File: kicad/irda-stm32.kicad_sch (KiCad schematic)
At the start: 33 parts, among them J1 USB_C_Receptacle_USB2.0_16P, J2 UART, J3 SWD, SW1 BOOT0_BUT, SW2 NRST_BUT, U1 TLV1117LV33DCYR, U2 STM32F042K6Tx, U3 TFBS4711

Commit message: update kicad, idk
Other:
- note added: "Alternative STM32C071FBP6 Slightly better/cheaper part but F042 is more available. F042Fxxx overlaps USB/UART1 which means its unuseable."
- note removed: "Alternative STM32C071FBPx Slightly better/cheaper part but F042 is more available. F042F overlaps USB/UART1 which means its unuseable."
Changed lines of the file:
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@@
 		)
 	)
-	(text "Alternative\nSTM32C071FBPx\n\nSlightly better/cheaper part but F042 is more available.\n\nF042F overlaps USB/UART1 which means its unuseable."
+	(text "Alternative\nSTM32C071FBP6\n\nSlightly better/cheaper part but F042 is more available.\n\nF042Fxxx overlaps USB/UART1 which means its unuseable."
 		(exclude_from_sim no)
 		(at 102.362 147.32 0)

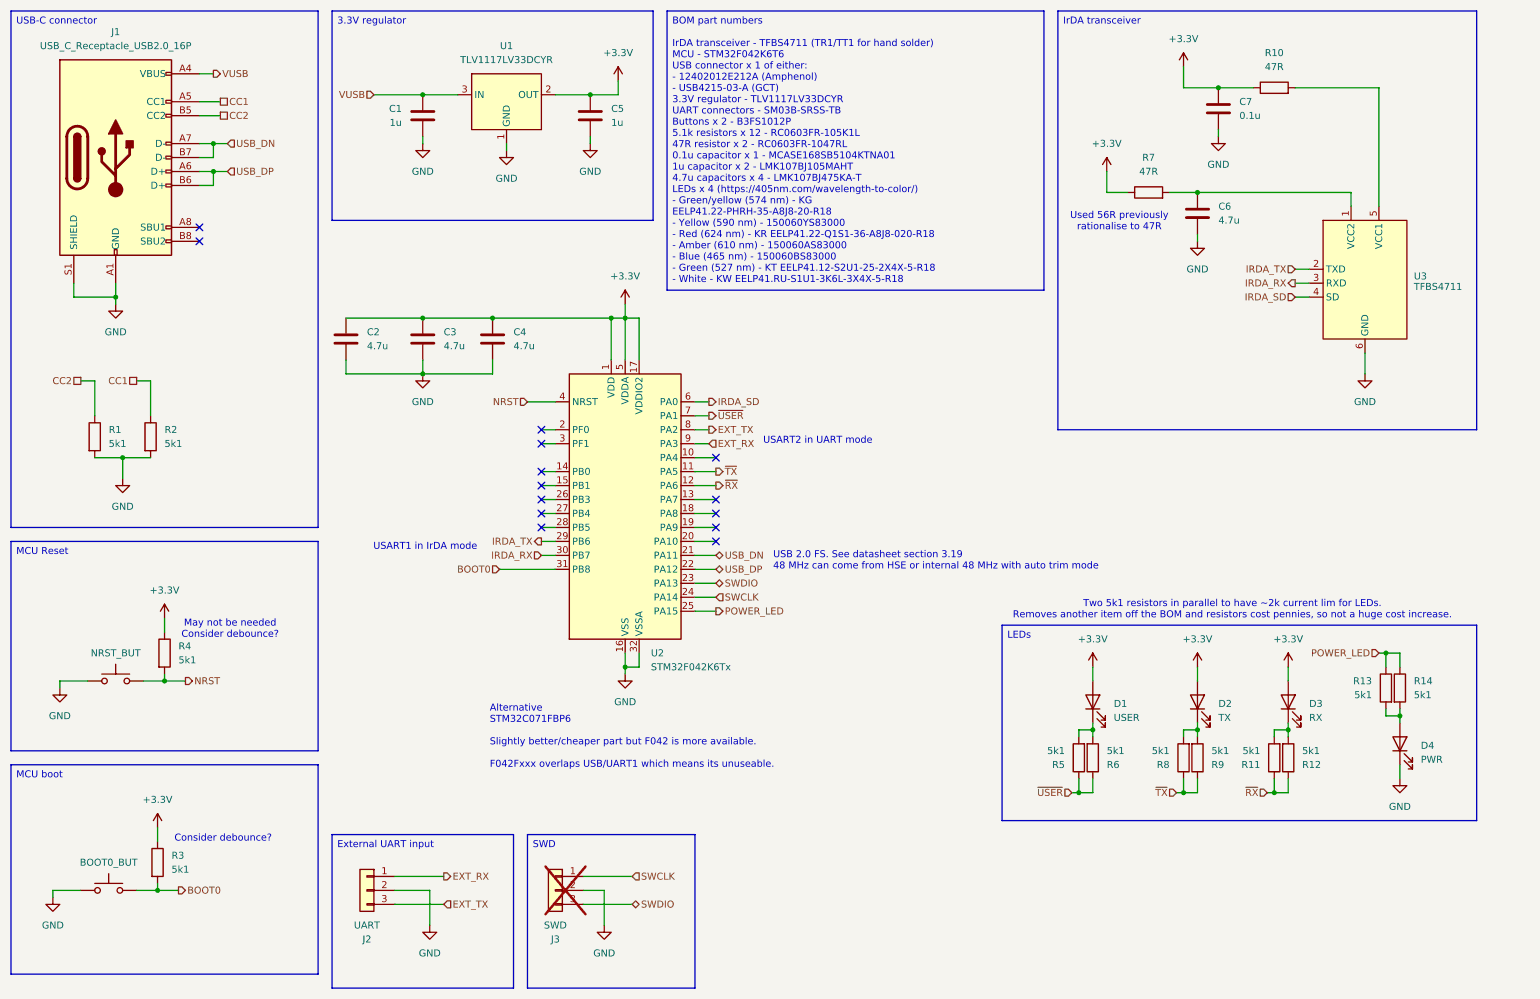
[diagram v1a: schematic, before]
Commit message: update PCB for c071fbp6
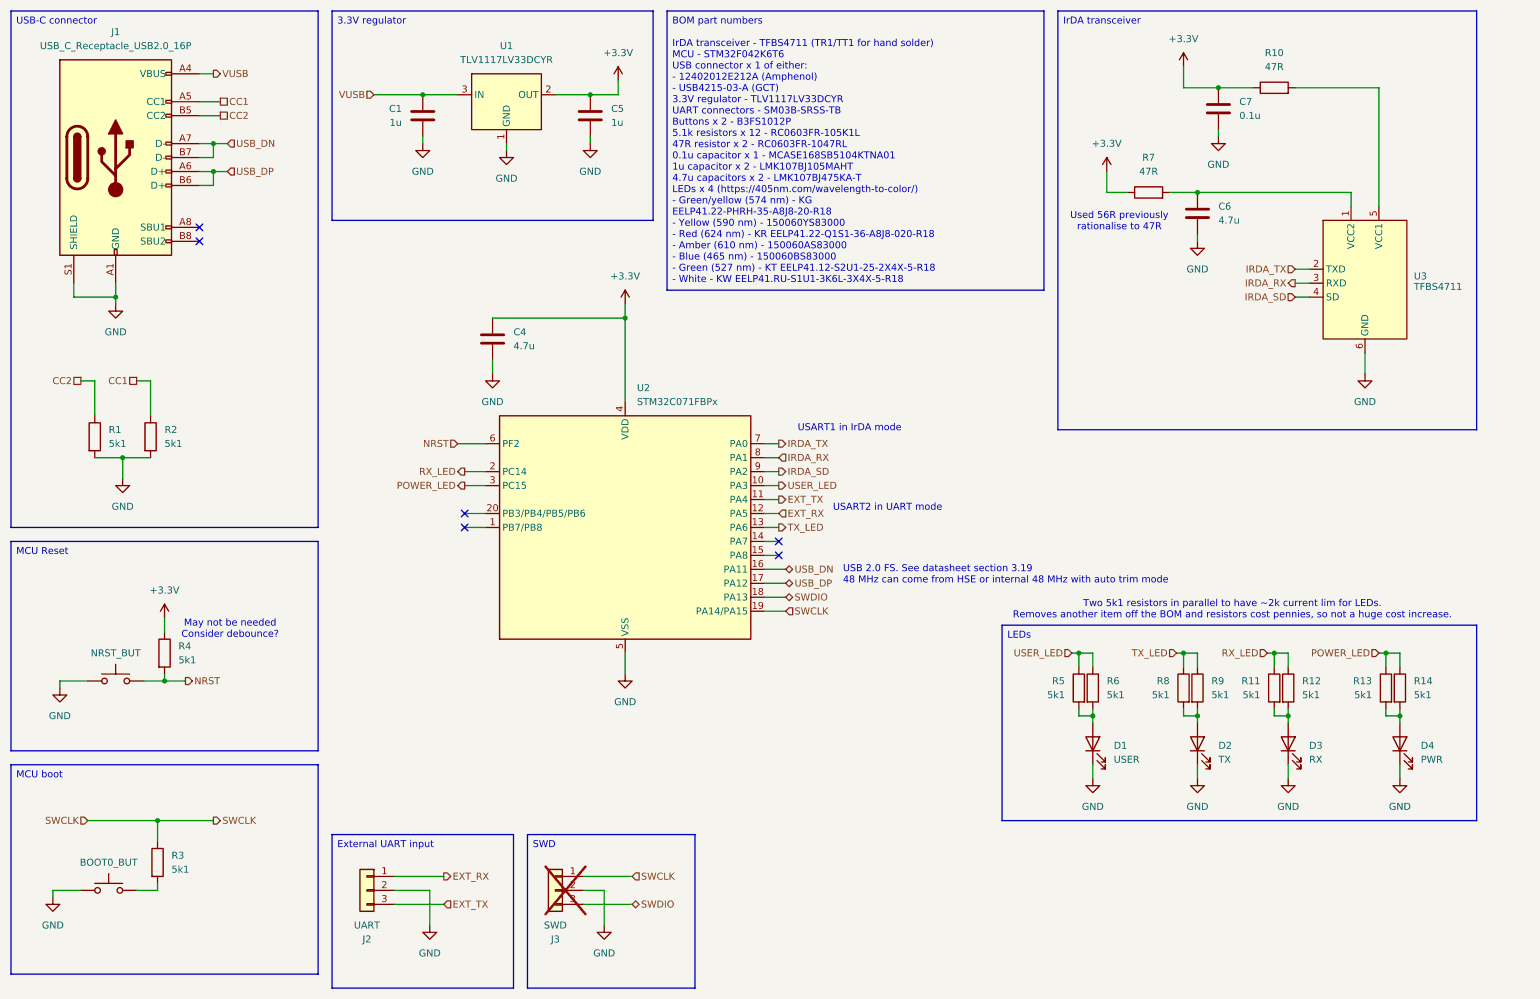
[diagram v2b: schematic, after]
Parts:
- removed C2, C3: 4.7u, Capacitor_SMD:C_0603_1608Metric, symbol Device:C
- removed U2: STM32F042K6Tx, Package_QFP:LQFP-32_7x7mm_P0.8mm, symbol MCU_ST_STM32F0:STM32F042K6Tx
- added U2: STM32C071FBPx, Package_SO:TSSOP-20_4.4x6.5mm_P0.65mm, symbol MCU_ST_STM32C0:STM32C071FBPx
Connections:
- net +3.3V: now also U2.4 (VDD); no longer D1.2 (A), D2.2 (A), D3.2 (A), R3.1
- net EXT_RX: now also U2.12 (PA5)
- net EXT_TX: now also U2.11 (PA4)
- net GND: now also D1.1 (K), D2.1 (K), D3.1 (K), U2.5 (VSS)
- net IRDA_RX: now also U2.8 (PA1)
- net IRDA_SD: now also U2.9 (PA2)
- net IRDA_TX: now also U2.7 (PA0)
- net NRST: now also U2.6 (PF2)
- net POWER_LED: now also U2.3 (PC15)
- net SWCLK: now also R3.1, U2.19 (PA14/PA15)
- net SWDIO: now also U2.18 (PA13)
- net USB_DN: now also U2.16 (PA11)
- net USB_DP: now also U2.17 (PA12)
- net at R8.2, R9.2: now also D2.2 (A); no longer D2.1 (K)
- net at R5.2, R6.2: now also D1.2 (A); no longer D1.1 (K)
- net at R11.2, R12.2: now also D3.2 (A); no longer D3.1 (K)
- net BOOT0: no longer names the net of R3.2, SW1.2
- net ~{RX} renamed RX_LED
- net RX_LED: now also U2.2 (PC14)
- net ~{TX} renamed TX_LED
- net TX_LED: now also U2.13 (PA6)
- net ~{USER} renamed USER_LED
- net USER_LED: now also U2.10 (PA3)
- no-connect marks 14 -> 6
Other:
- note removed: "Alternative STM32C071FBP6 Slightly better/cheaper part but F042 is more available. F042Fxxx overlaps USB/UART1 which means its unuseable."
- note removed: "Consider debounce?"
- moved on the sheet: D1, D2, D3, R11, R12, R5, R6, R8, R9

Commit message: fix BOOT0 button and USB ground
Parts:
- added C6: 0.1u, Capacitor_SMD:C_0603_1608Metric, symbol Device:C
- added TP1: NRST, Connector_PinHeader_2.54mm:PinHeader_1x01_P2.54mm_Vertical, symbol Connector:TestPoint
- renumbered C7 to C1, C6 to C2, C1 to C3, C5 to C4, C4 to C5, R10 to R1, R11 to R10, R12 to R11, R13 to R12, R14 to R13, R3 to R14, R7 to R2, R1 to R3, R2 to R4, R4 to R5, R5 to R6, R6 to R7, SW2 to SW1, SW1 to SW2, U3 to U2, U2 to U3
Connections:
- net +3.3V: now also SW2.2
- net GND: now also R14.2, C6.2; no longer SW2.1
- net NRST: now also C6.1, TP1.1
- net SWCLK: now also SW2.1
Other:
- note removed: "May not be needed Consider debounce?"
- moved on the sheet: R14, R5

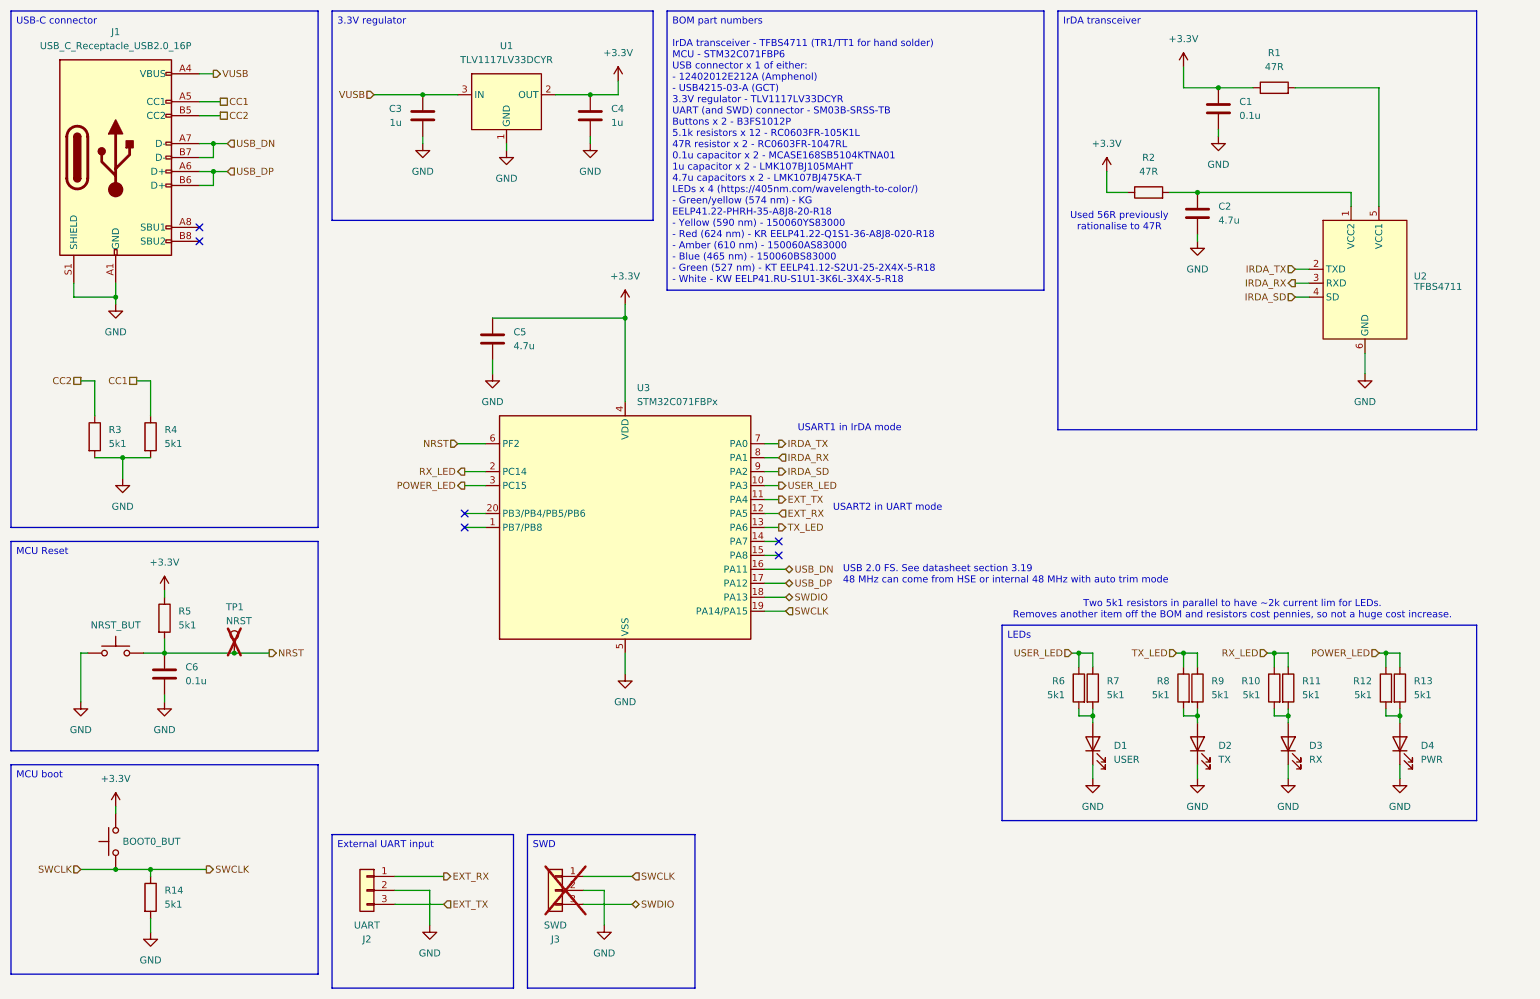
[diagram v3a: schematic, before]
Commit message: add lcsc/jlc part numbers and fix ir filters
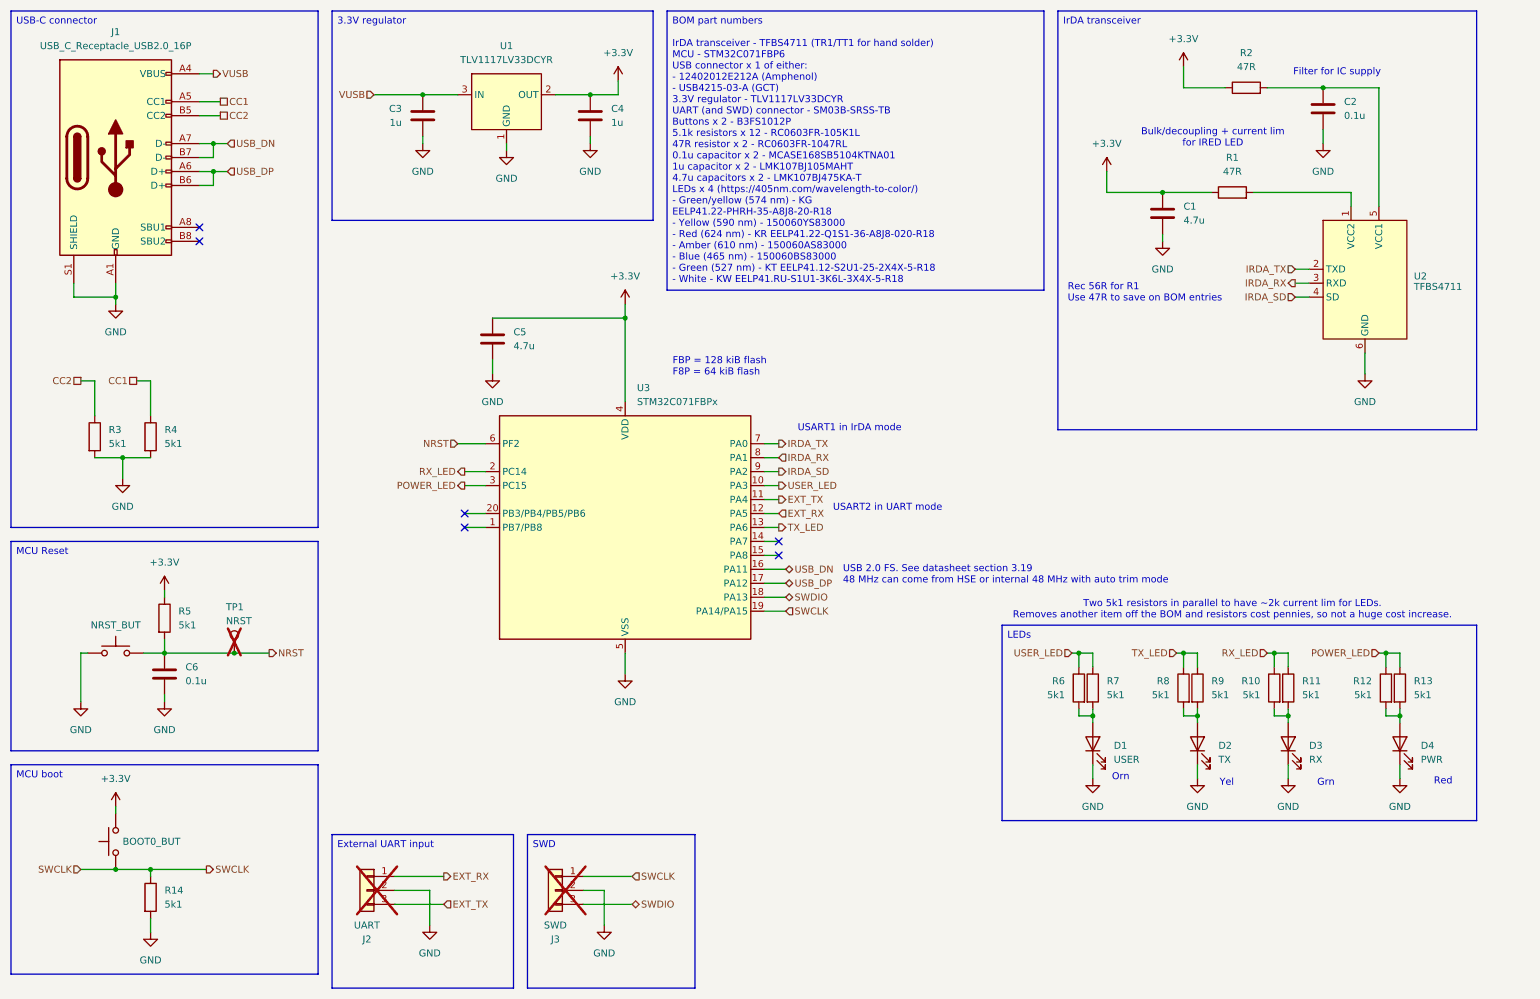
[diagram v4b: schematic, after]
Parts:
- C1: renamed from C2; LCSC Part # (none) -> C162274
- C2: renamed from C1; LCSC Part # (none) -> C77055
- C3, C4: LCSC Part # (none) -> C85862
- C5: LCSC Part # (none) -> C162274
- C6: LCSC Part # (none) -> C77055
- D1: LCSC Part # (none) -> C84269
- D2: LCSC Part # (none) -> C965802
- D3: LCSC Part # (none) -> C965804
- D4: LCSC Part # (none) -> C965799
- J1: LCSC Part # (none) -> C165948
- J2: LCSC Part # (none) -> C160403; now not fitted; now left out of the parts list
- J3: LCSC Part # (none) -> C160403; now left out of the parts list
- R1: renamed from R2; LCSC Part # (none) -> C114623
- R10, R11, R12, R13, R14, R3, R4, R5, R6, R7, R8, R9: LCSC Part # (none) -> C105580
- R2: renamed from R1; LCSC Part # (none) -> C114623
- SW1, SW2: LCSC Part # (none) -> C271753
- U1: LCSC Part # (none) -> C15578
- U2: LCSC Part # (none) -> C3171514
- U3: LCSC Part # (none) -> C41835018
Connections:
- net +3.3V: now also C1.1; no longer C2.1
- net at R1.2, U2.1 (VCC2): no longer C1.1
- net at R2.2, U2.5 (VCC1): now also C2.1
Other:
- note added: "Bulk/decoupling + current lim for IRED LED"
- note added: "FBP = 128 kiB flash F8P = 64 kiB flash"
- note added: "Filter for IC supply"
- note added: "Grn"
- note added: "Orn"
- note added: "Rec 56R for R1 Use 47R to save on BOM entries"
- note added: "Red"
- note added: "Yel"
- note removed: "Used 56R previously rationalise to 47R"
- company: (none) -> mamba2410
- title: (none) -> USB to IrDA
- moved on the sheet: C1, C2, R1, R2
